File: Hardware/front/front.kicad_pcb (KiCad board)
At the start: 4 copper layers, 70 x 60 mm, 17 parts, among them J101 Conn_02x10_Odd_Even, J102 Conn_02x08_Odd_Even, U101 XRA1203, U102 AT24CS32-SSHM, U103 PCA9955B

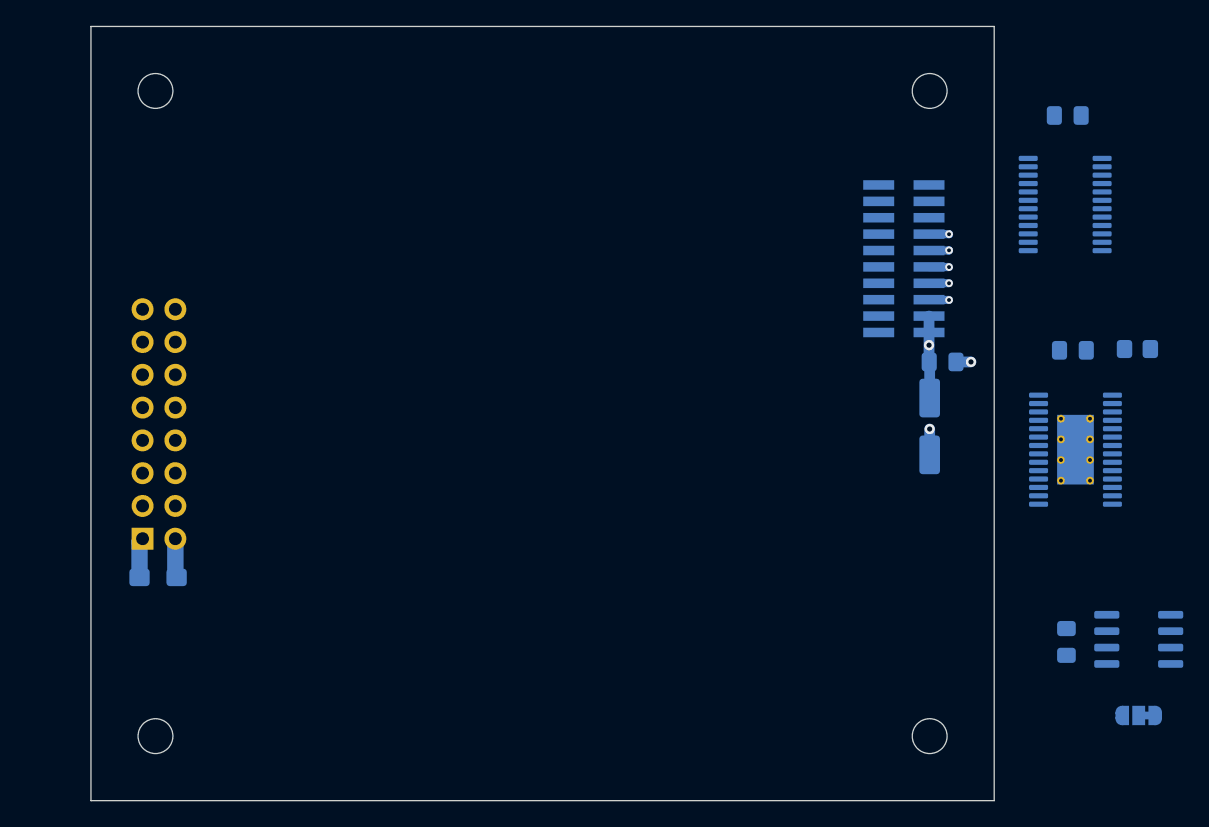
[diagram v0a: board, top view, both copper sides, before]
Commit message: Finished front panel board
- Added all the switches/encoders required for the front panel, as well
  as the indicators. They are in (roughly? hopefully lol) the right
  places for the current front panel design.

  The PCB shall be mounted on 4x 8mm standoffs with M2 screws.
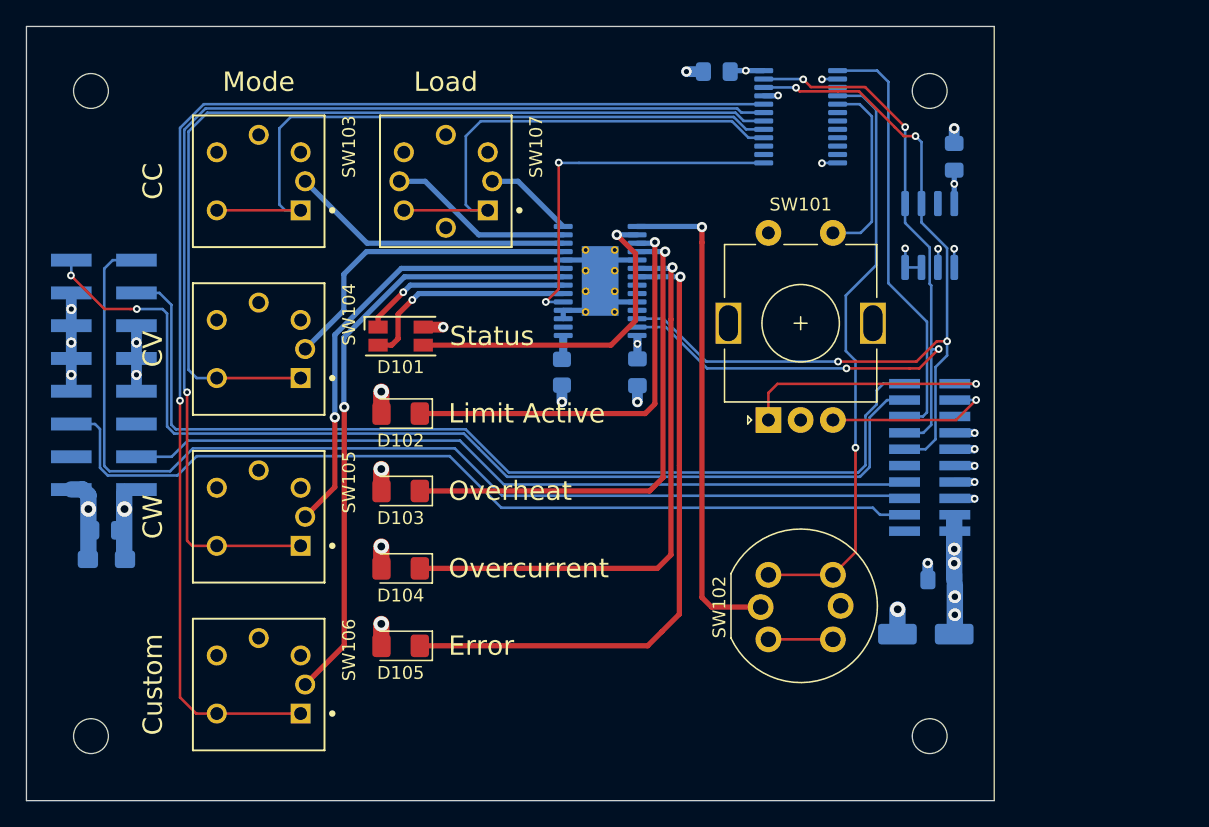
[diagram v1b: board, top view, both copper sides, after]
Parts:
- removed JP101: Cfg WP, Jumper:SolderJumper-3_P1.3mm_Bridged12_RoundedPad1.0x1.5mm
- added C107: 100nF, Capacitor_SMD:C_0805_2012Metric_Pad1.18x1.45mm_HandSolder, B.Cu at (21.1, 59.0)
- added D101: LED_RGBA, LED_SMD:LED_RGB_1210, F.Cu at (44.0, 44.0)
- added D102: Amber, LED_SMD:LED_1206_3216Metric_Pad1.42x1.75mm_HandSolder, F.Cu at (44.0, 50.0)
- added D103: Red, LED_SMD:LED_1206_3216Metric_Pad1.42x1.75mm_HandSolder, F.Cu at (44.0, 56.0)
- added D104: Red, LED_SMD:LED_1206_3216Metric_Pad1.42x1.75mm_HandSolder, F.Cu at (44.0, 62.0)
- added D105: Red, LED_SMD:LED_1206_3216Metric_Pad1.42x1.75mm_HandSolder, F.Cu at (44.0, 68.0)
- added SW101: Alps EC11E, Rotary_Encoder:RotaryEncoder_Alps_EC11E-Switch_Vertical_H20mm, F.Cu at (72.5, 50.5)
- added SW102: C&K-D6R-Illuminated, programmable-load:C&K-D6R-LED, F.Cu at (75.0, 65.0)
- added SW103: B3W-9002-Y1C, programmable-load:Omron-B3W-90XX-X1X, F.Cu at (33.0, 32.0)
- added SW104: B3W-9002-Y1C, programmable-load:Omron-B3W-90XX-X1X, F.Cu at (33.0, 45.0)
- added SW105: B3W-9002-Y1C, programmable-load:Omron-B3W-90XX-X1X, F.Cu at (33.0, 58.0)
- added SW106: B3W-9002-Y1C, programmable-load:Omron-B3W-90XX-X1X, F.Cu at (33.0, 71.0)
- added SW107: B3W-9000-RHG2C, programmable-load:Omron-B3W-90XX-X2X, F.Cu at (47.5, 32.0)
- J102: footprint Connector_PinHeader_2.54mm:PinHeader_2x08_P2.54mm_Vertical -> Connector_PinHeader_2.54mm:PinHeader_2x08_P2.54mm_Vertical_SMD
- moved R101 44.6 mm to (56.5, 46.8), turned to 90 degrees
- moved U103 39.1 mm to (59.5, 39.7), turned to 0 degrees
- moved C105 38.6 mm to (86.9, 30.1), turned to 90 degrees
- moved U102 35.2 mm to (85.0, 36.2), turned to 90 degrees
- moved C106 33.8 mm to (62.4, 46.8), turned to 90 degrees
- moved C104 27.4 mm to (68.5, 23.5), turned to 0 degrees
- moved U101 21.6 mm to (75.0, 27.0)
- moved C101 16.9 mm to (85.9, 62.9), turned to 180 degrees
- moved C102 16.1 mm to (84.7, 67.1), turned to 180 degrees
- moved J101 15.5 mm to (85.0, 53.4)
- moved J102 13.0 mm to (21.0, 47.0)
- moved H101 5.00 mm to (20.0, 25.0)
- moved H104 5.00 mm to (20.0, 75.0)
- moved C103 4.24 mm to (21.2, 61.3)
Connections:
- net /~{DISP_RESET} renamed /~{RESET}
- U101 pad 13: unconnected-(U101-Pad13) -> /~{LED_OE}
- U101 pad 16: unconnected-(U101-Pad16) -> /SW_ENABLE
- U101 pad 17: unconnected-(U101-Pad17) -> /SW_MODE_CC
- U101 pad 18: unconnected-(U101-Pad18) -> /SW_MODE_CV
- U101 pad 19: unconnected-(U101-Pad19) -> /SW_MODE_CW
- U101 pad 20: unconnected-(U101-Pad20) -> /SW_MODE_EXT
- U101 pad 3: +3V3 -> unconnected-(U101-Pad3)
- U101 pad 4: unconnected-(U101-Pad4) -> /SW_MENU
- U101 pad 5: unconnected-(U101-Pad5) -> /SW_ENCODER
- U103 pad 11: unconnected-(U103-Pad11) -> /LED_MODE_CV
- U103 pad 12: unconnected-(U103-Pad12) -> /LED_MODE_CC
- U103 pad 13: unconnected-(U103-Pad13) -> /LED_EN_G
- U103 pad 14: unconnected-(U103-Pad14) -> /LED_EN_R
- U103 pad 15: unconnected-(U103-Pad15) -> /LED_MENU
- U103 pad 16: unconnected-(U103-Pad16) -> /LED_STATUS_B
- U103 pad 17: unconnected-(U103-Pad17) -> /LED_LIMITING
- U103 pad 18: unconnected-(U103-Pad18) -> /LED_OVRHEAT
- U103 pad 20: unconnected-(U103-Pad20) -> /LED_OVRCURR
- U103 pad 21: unconnected-(U103-Pad21) -> /LED_ERROR
- U103 pad 25: +3V3 -> unconnected-(U103-Pad25)
- U103 pad 6: unconnected-(U103-Pad6) -> /LED_STATUS_G
- U103 pad 7: unconnected-(U103-Pad7) -> /LED_STATUS_R
- U103 pad 8: unconnected-(U103-Pad8) -> /LED_MODE_EXT
- U103 pad 9: unconnected-(U103-Pad9) -> /LED_MODE_CW
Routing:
- net /SW_MODE_EXT: track 0.00 -> 100.0 mm, vias 0 -> 1
- net /SW_MODE_CW: track 0.00 -> 86.6 mm, vias 0 -> 1
- net /~{DISP_CS}: track 0.00 -> 82.6 mm
- net /~{RESET}: track 0.00 -> 82.1 mm, vias 0 -> 2
- net /DISP_D/~{C}: track 0.00 -> 76.5 mm
- net /SW_MODE_CV: track 0.00 -> 72.9 mm
- net /DISP_MOSI: track 0.00 -> 70.5 mm
- net /SCL: track 0.00 -> 67.0 mm, vias 0 -> 4
- net /SDA: track 0.00 -> 64.6 mm, vias 0 -> 4
- net /DISP_SCK: track 0.00 -> 61.5 mm
- net /SW_MODE_CC: track 0.00 -> 52.5 mm
- net /LED_ERROR: track 0.00 -> 50.7 mm, vias 0 -> 1
- net /LED_MODE_EXT: track 0.00 -> 47.1 mm, vias 0 -> 1
- net /SW_MENU: track 0.00 -> 46.5 mm, vias 0 -> 1
- net /LED_OVRCURR: track 0.00 -> 45.0 mm, vias 0 -> 1
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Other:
- board size 70 x 60 mm -> 75 x 60 mm
- board text added: "2022 Tristan Seifert"
- board text added: "CC"
- board text added: "CV"
- board text added: "CW"
- board text added: "Custom"
- board text added: "Error"
- board text added: "JLCJLCJLCJLC"
- board text added: "Limit Active"
- board text added: "Load"
- board text added: "Mode"
- board text added: "Overcurrent"
- board text added: "Overheat"
- board text added: "Programmable Load HMI"
- board text added: "Rev 1"
- board text added: "Status"

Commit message: Front panel layout tweaks
- Made space for a ~38mm diameter knob on the rotary encoder, by moving
  the indicators and menu button somewhat.
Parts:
- added R102: 10k, Resistor_SMD:R_0805_2012Metric_Pad1.20x1.40mm_HandSolder, B.Cu at (75.0, 34.0)
- moved D101 8.00 mm to (44.0, 52.0)
- moved D102 8.00 mm to (44.0, 58.0)
- moved D103 8.00 mm to (44.0, 64.0)
- moved D104 8.00 mm to (44.0, 70.0)
- moved D105 8.00 mm to (44.0, 76.0)
- moved SW102 5.00 mm to (75.0, 70.0)
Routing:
- net /LED_ERROR: track 50.7 -> 59.6 mm
- net /LED_STATUS_R: track 16.1 -> 24.1 mm
- net /LED_OVRHEAT: track 39.0 -> 47.0 mm
- net /LED_STATUS_G: track 17.1 -> 25.1 mm
- net /LED_OVRCURR: track 45.0 -> 52.9 mm
- net /LED_LIMITING: track 32.5 -> 40.4 mm
- net /~{IRQ}: track 33.0 -> 38.8 mm, vias 0 -> 2
- net /SW_MENU: track 46.5 -> 52.2 mm
- net /LED_STATUS_B: track 26.1 -> 31.7 mm
- net /LED_MENU: track 38.6 -> 43.4 mm
- net +3V3: track 28.4 -> 29.6 mm, vias 13 -> 14

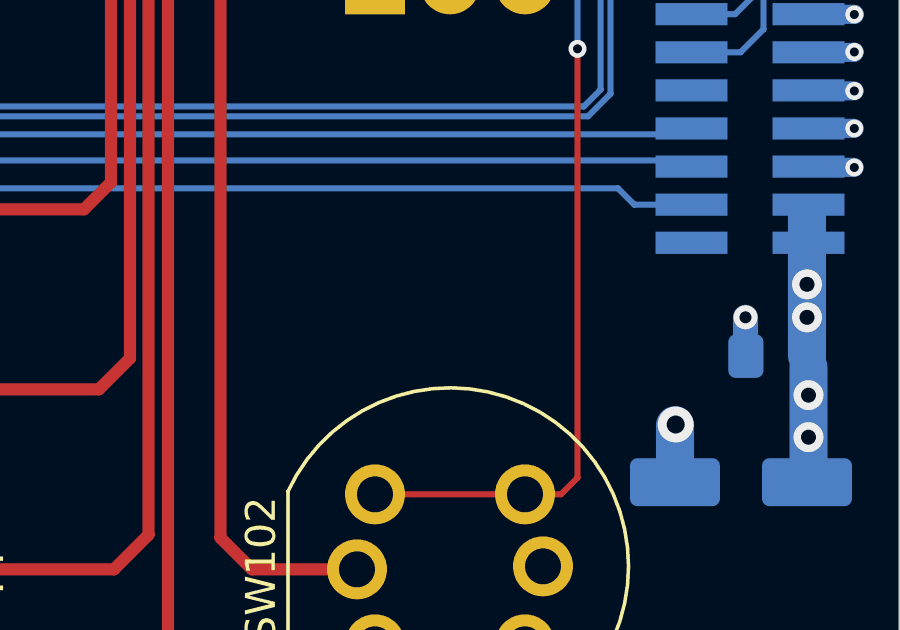
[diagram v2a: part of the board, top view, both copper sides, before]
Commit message: More tweaks to controller board
- Moved a few components around to make more space for cables from front
  panel jacks; namely, the beeper and front panel connector were moved
  somewhat and traces cleaned up
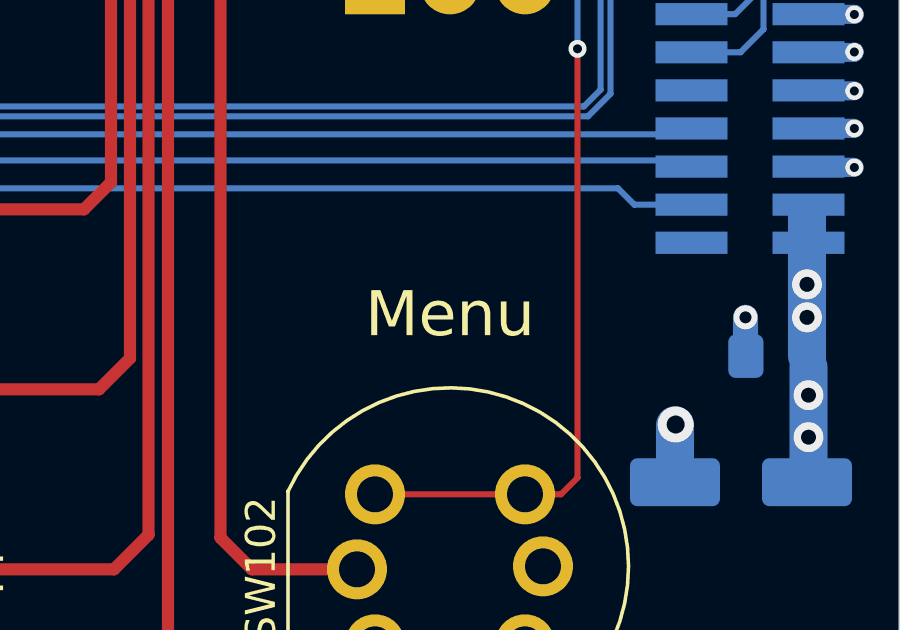
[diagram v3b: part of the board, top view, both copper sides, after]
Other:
- board text added: "Menu"
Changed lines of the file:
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@@
     (effects (font (size 1.3 1.3) (thickness 0.2)) (justify mirror))
   )
-  (gr_text "2022 Tristan Seifert" (at 58.5 60.2) (layer "B.SilkS")
+  (gr_text "2022 Tristan Seifert" (at 58.5 61.3) (layer "B.SilkS")
     (effects (font (size 1.74 1.74) (thickness 0.2)) (justify mirror))
   )
-  (gr_text "Rev 1" (at 58.5 63) (layer "B.SilkS")
-    (effects (font (size 1.74 1.74) (thickness 0.2) italic) (justify mirror))
+  (gr_text "Rev 1" (at 58.5 64.1) (layer "B.SilkS")
+    (effects (font (size 1.74 1.74) (thickness 0.2)) (justify mirror))
   )
   (gr_text "JLCJLCJLCJLC" (at 20.9 47.05 90) (layer "B.SilkS")
     (effects (font (size 1 1) (thickness 0.15)) (justify mirror))
   )
-  (gr_text "Programmable Load HMI" (at 58.5 57) (layer "B.SilkS")
-    (effects (font (size 2 2) (thickness 0.3)) (justify mirror))
+  (gr_text "Programmable Load HMI" (at 58.5 58) (layer "B.SilkS")
+    (effects (font (size 2 2) (thickness 0.3) italic) (justify mirror))
   )
   (gr_text "Mode" (at 33 24.3) (layer "F.SilkS")
@@
     (effects (font (size 1.5 1.5) (thickness 0.15)) (justify left))
   )
+  (gr_text "Menu" (at 75 61.5) (layer "F.SilkS")
+    (effects (font (size 1.5 1.5) (thickness 0.2)))
+  )
   (gr_text "CW" (at 24.8 58 90) (layer "F.SilkS")

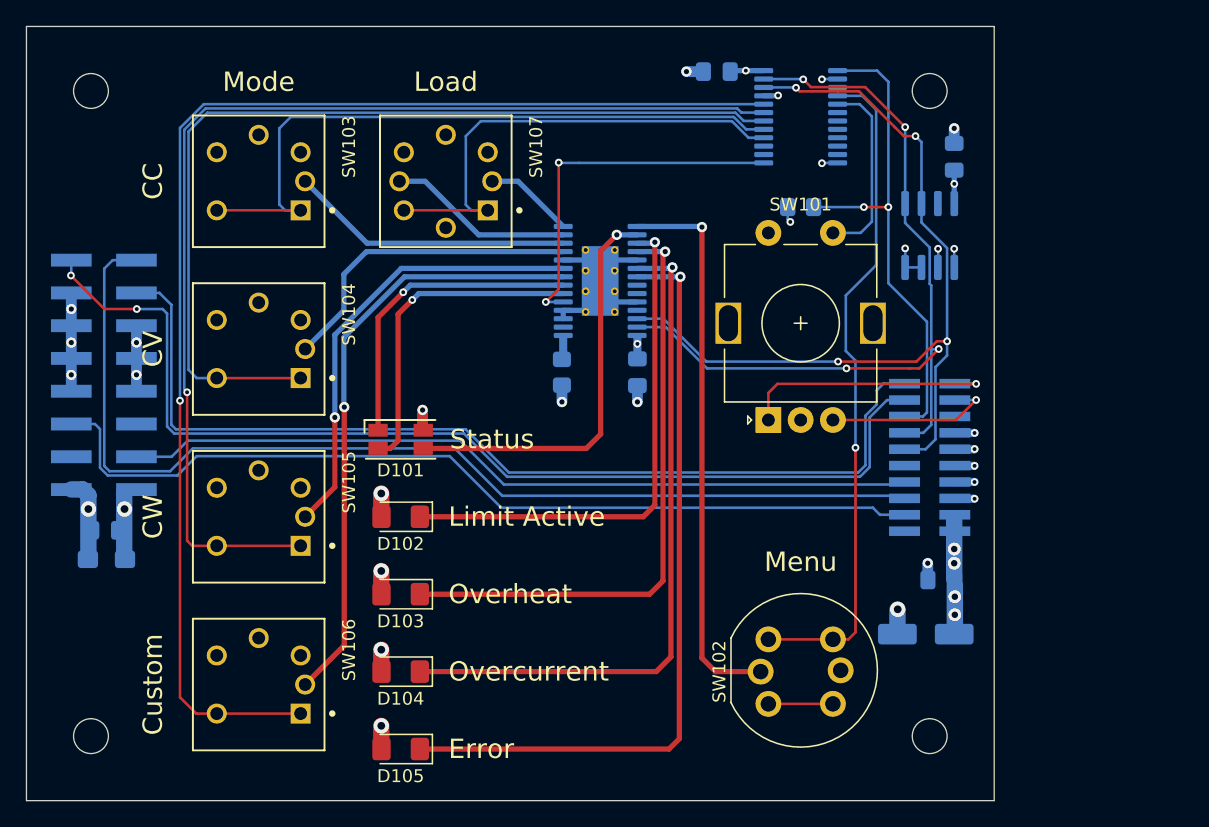
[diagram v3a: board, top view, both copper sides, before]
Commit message: Tweaks to front and rear panel boards
- Minor movement of stuff and silkscreen cleanup for manufacturing
  exporting

- Removed display connector from front panel board; this is now directly
  connected to the controller instead, to make the board a bit simpler
  and reduce the amount of stuff going on
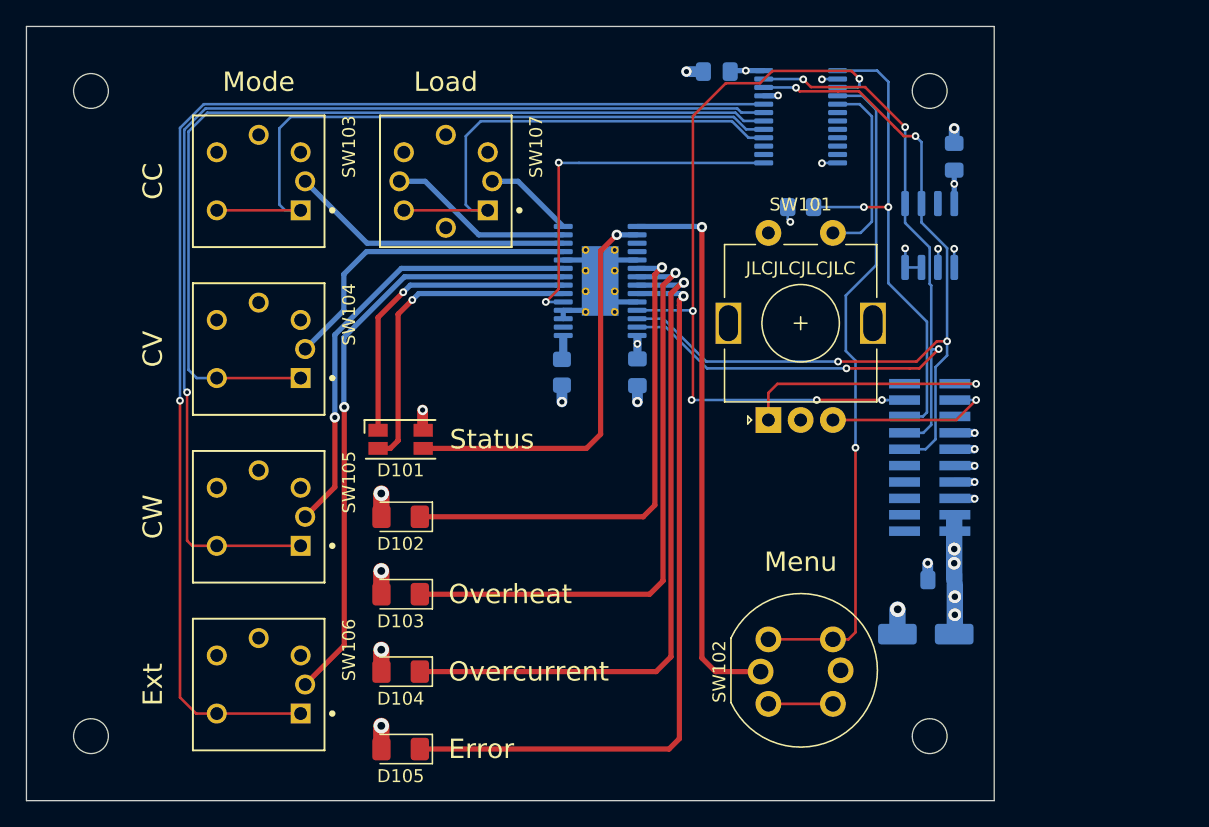
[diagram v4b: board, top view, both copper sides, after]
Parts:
- removed C103: 10µF, Capacitor_Tantalum_SMD:CP_EIA-3216-18_Kemet-A_Pad1.58x1.35mm_HandSolder
- removed C107: 100nF, Capacitor_SMD:C_0805_2012Metric_Pad1.18x1.45mm_HandSolder
- removed J102: Conn_02x08_Odd_Even, Connector_PinHeader_2.54mm:PinHeader_2x08_P2.54mm_Vertical_SMD
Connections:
- J101 pad 12: /DISP_MISO -> unconnected-(J101-Pad12)
- J101 pad 14: /DISP_SCK -> unconnected-(J101-Pad14)
- J101 pad 16: /~{DISP_CS} -> unconnected-(J101-Pad16)
- J101 pad 18: /DISP_MOSI -> unconnected-(J101-Pad18)
- J101 pad 2: /DISP_D/~{C} -> unconnected-(J101-Pad2)
- U101 pad 3: unconnected-(U101-Pad3) -> /~{RESET}
- U103 pad 17: /LED_LIMITING -> unconnected-(U103-Pad17)
- U103 pad 18: /LED_OVRHEAT -> unconnected-(U103-Pad18)
- U103 pad 20: /LED_OVRCURR -> /LED_LIMITING
- U103 pad 21: /LED_ERROR -> /LED_OVRHEAT
- U103 pad 22: unconnected-(U103-Pad22) -> /LED_OVRCURR
- U103 pad 23: unconnected-(U103-Pad23) -> /LED_ERROR
- U103 pad 25: unconnected-(U103-Pad25) -> /~{RESET}
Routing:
- net /~{DISP_CS}: track 82.6 -> 0.00 mm
- net /DISP_D/~{C}: track 76.5 -> 0.00 mm
- net /DISP_MOSI: track 70.5 -> 0.00 mm
- net /DISP_SCK: track 61.5 -> 0.00 mm
- net /~{RESET}: track 82.1 -> 59.8 mm, vias 2 -> 5
- net GND: track 55.6 -> 36.6 mm, vias 23 -> 17
- net +3V3: track 29.6 -> 24.5 mm, vias 14 -> 13
- net /LED_LIMITING: track 40.4 -> 39.2 mm
- net /LED_ERROR: track 59.6 -> 58.6 mm
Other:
- board text added: "Ext"
- board text removed: "Custom"
- board text removed: "Limit Active"
- board text removed: "To ER-OLEDM032-1"
